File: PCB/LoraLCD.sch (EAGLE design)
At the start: 79 parts, among them IC1 STM32F767ZIT6, IC2 24AA025E64T-I/OT, IC5 TPS613222ADBVR, Q1 SSM3J338R,LF, Q2 SSM3J338R,LF, Q3 SSM3J338R,LF, Q4 SSM3J338R,LF, Q5 SSM3J338R,LF, U1 LORA-868MHZ

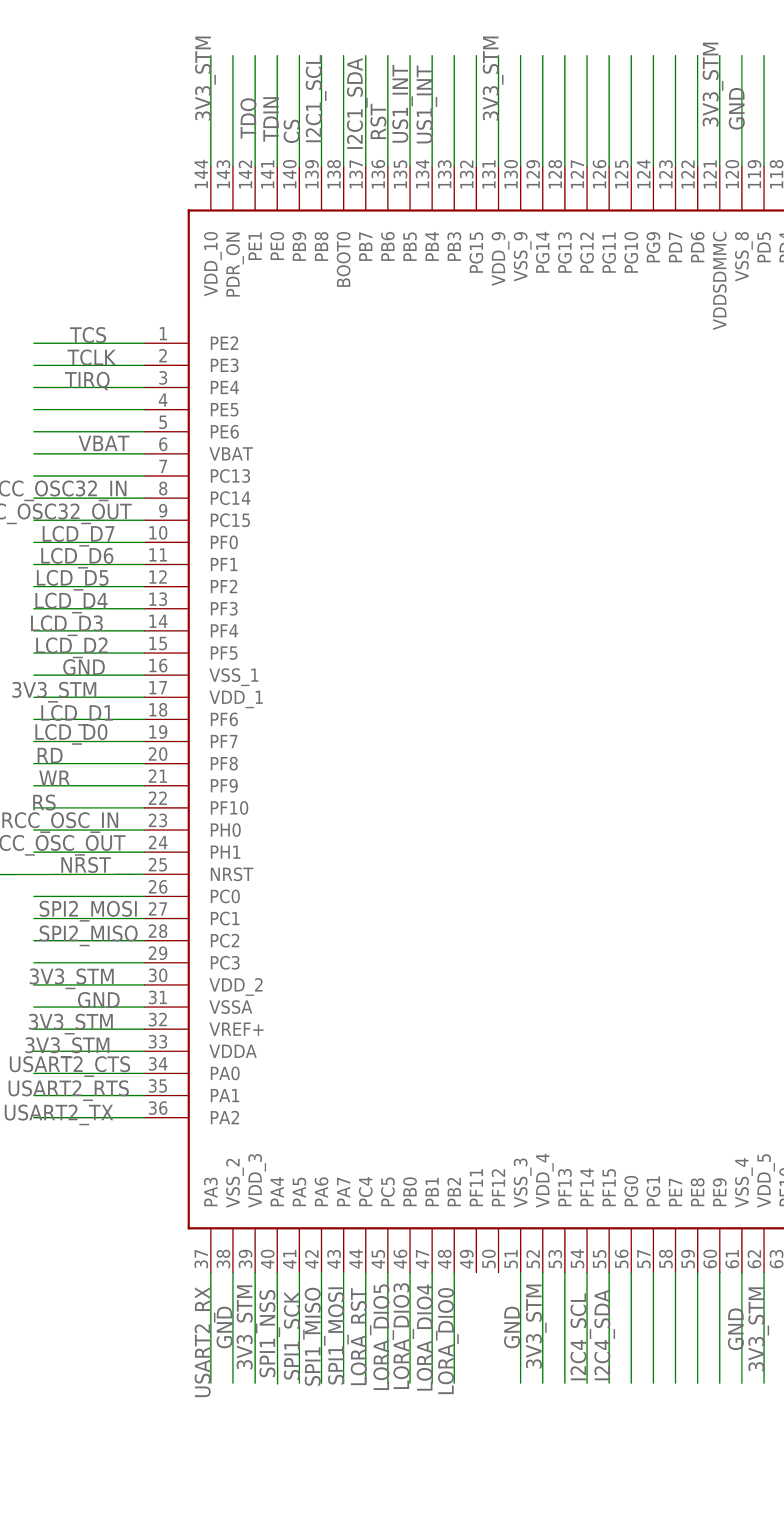
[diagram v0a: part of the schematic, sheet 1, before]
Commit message: fix 2 pin CS and RTS in control pin for LCD
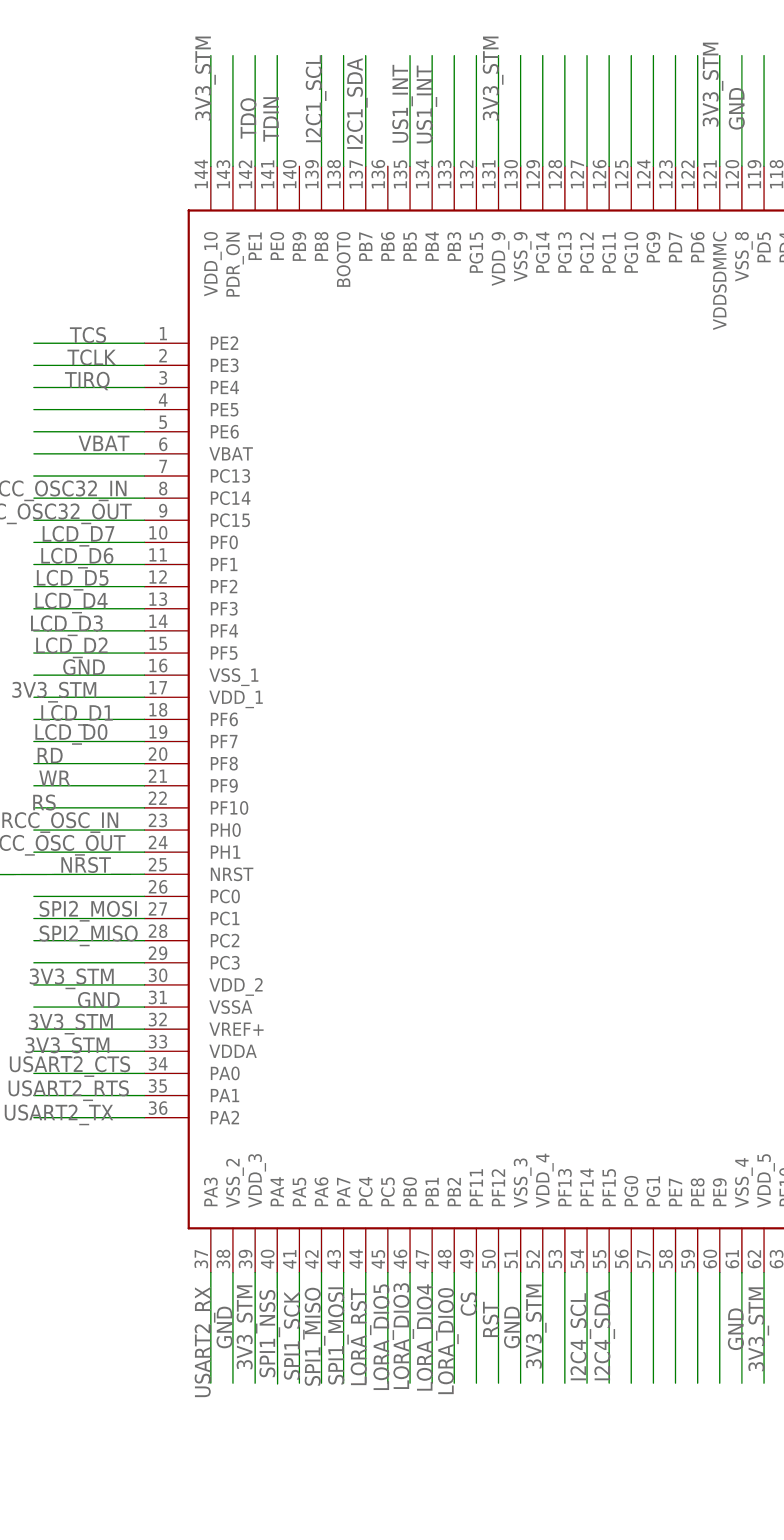
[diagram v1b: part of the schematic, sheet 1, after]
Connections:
- net CS: now also IC1.PF11; no longer IC1.PB9
- net RST: now also IC1.PF12; no longer IC1.PB6
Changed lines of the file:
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@@
 </layers>
 <schematic xreflabel="%F%N/%S.%C%R" xrefpart="/%S.%C%R">
+<fusionteam huburn="a.YnVzaW5lc3M6aGF3aGFtYnVyZzE2MA" projecturn="a.YnVzaW5lc3M6aGF3aGFtYnVyZzE2MCMyMDIwMDMxODI3NjA2OTk3Ng" folderUrn="urn:adsk.wipprod:fs.folder:co.goNDv-9XQGeF0P4ml8q09Q" urn="urn:adsk.wipprod:dm.lineage:v_c-DKWzSUawachcDsm0LA"  versionUrn="urn:adsk.wipprod:fs.file:vf.v_c-DKWzSUawachcDsm0LA?version=1" camFileUrn="" camFileVersionUrn="" lastpublishedchangeguid="babf9d0b-71c7-e20c-f1f4-92fc3aea1251"/>
 <attributes>
 </attributes>
@@
 </segment>
 </net>
-<net name="CS" class="0">
-<segment>
-<pinref part="IC1" gate="G$1" pin="PB9"/>
-<wire x1="38.1" y1="96.52" x2="38.1" y2="109.22" width="0.1524" layer="91"/>
-<label x="38.1" y="99.06" size="1.778" layer="95" rot="R90"/>
-</segment>
-</net>
 <net name="N$53" class="0">
 <segment>
@@
 </segment>
 </net>
+<net name="CS" class="0">
+<segment>
+<pinref part="IC1" gate="G$1" pin="PF11"/>
+<wire x1="58.42" y1="-30.48" x2="58.42" y2="-43.18" width="0.1524" layer="91"/>
+<label x="58.42" y="-35.56" size="1.778" layer="95" rot="R90"/>
+</segment>
+</net>
 <net name="RST" class="0">
 <segment>
-<pinref part="IC1" gate="G$1" pin="PB6"/>
-<wire x1="48.26" y1="96.52" x2="48.26" y2="109.22" width="0.1524" layer="91"/>
-<label x="48.06" y="99.42" size="1.778" layer="95" rot="R90"/>
-</segment>
-</net>
+<pinref part="IC1" gate="G$1" pin="PF12"/>
+<wire x1="60.96" y1="-30.48" x2="60.96" y2="-43.18" width="0.1524" layer="91"/>
+<label x="60.96" y="-38.1" size="1.778" layer="95" rot="R90"/>
+</segment>
+</net>
